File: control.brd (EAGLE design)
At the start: 100 x 80 mm, 60 parts, among them IC1 OPA336P, IC2 XMEGA16A4A, IC3 LM317MBSTT3, IC4 OPA336P, Q1 BSS123, Q2 BSS123, Q3 BC548, Q4 BC557C, Q5 TIP41C, Q6 TIP42C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

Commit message: noch falsche layer
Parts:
- removed IC1, IC4: OPA336P, burr-brown:DIL08
- added C10, C9: (no value), resistor:E2,5-7
- added IC5: LM358N, linear:DIL08
- added R32, R33, R34, R35, R36, R37, R38, R39, R40, R41, R42, R43, R44, R45, R46, R47, R48: (no value), resistor:M0805
- added SV1, SV2: (no value), con-ml:ML6S
- moved C3 65.1 mm to (25.4, 31.8)
- moved C1 64.8 mm to (34.3, 36.8)
- moved JP6 64.3 mm to (8.89, 34.3)
- moved Q5 64.2 mm to (48.3, 7.62), turned to 270 degrees
- moved C2 63.2 mm to (16.5, 39.4)
- moved C4 63.2 mm to (22.9, 48.3)
- moved R18 63.2 mm to (16.5, 44.5)
- moved IC2 63.2 mm to (25.4, 39.4)
- moved Q6 60.2 mm to (48.3, 20.3), turned to 270 degrees
- moved JP4 59.9 mm to (22.9, 29.2)
- moved C7 59.9 mm to (41.9, 3.81), flipped to the bottom
- moved R13 53.0 mm to (41.9, 20.3), flipped to the bottom, turned to 0 degrees
- moved Q7 50.6 mm to (41.9, 16.5)
- moved R10 50.6 mm to (3.81, 45.7)
- moved R7 50.6 mm to (3.81, 49.5)
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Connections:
- removed net N$12: C7.1, Q5.E, R22.1
- new net DIS_A: IC2.20, Q1.1
- new net EN_A1: IC2.21, Q2.1
- new net EN_A2: IC2.22, Q8.1
- new net N$44: IC2.34, SV2.P$1
- net +12V: now also C9.+, IC5.8; no longer IC1.4, IC4.4
- net +3V3: now also SV2.P$2
- net ADC2: now also IC5.2; no longer IC1.2
- net ADC4: now also C10.+, C7.1, Q5.E, R22.1, R32.2
- net GND: now also C10.-, C9.-, IC5.4, R33.1, R34.1, R35.1, R36.1, R37.1, R38.1, R39.1, R40.1, SV2.P$6; no longer IC1.7, IC4.7
- net N$11: now also IC5.3; no longer IC1.3
- net N$17: now also SV2.P$5
- net N$18: now also R33.2, R41.1
- net N$19: now also R34.2, R42.1
- net N$20: now also R35.2, R43.1
- net N$21: now also R36.2, R44.1
- net N$22: now also R37.2, R45.1
- net N$23: now also R38.2, R46.1
- net N$24: now also R39.2, R47.1
- net N$25: now also R40.2, R48.1
- net N$28: now also IC5.7; no longer IC4.6
- net N$30: now also IC5.6; no longer IC4.2
- net N$31: now also IC5.5; no longer IC4.3
- net N$32: now also R32.1
- net N$9: now also IC5.1; no longer IC1.6
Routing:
- net N$32: track 11.7 -> 0.00 mm
- net N$30: track 8.53 -> 0.00 mm
- net N$28: track 8.27 -> 0.00 mm
- net ADC3: track 6.13 -> 14.3 mm
- net +12V: track 26.5 -> 34.0 mm, vias 0 -> 1
- net N$4: track 7.38 -> 0.54 mm
- net N$11: track 13.5 -> 6.94 mm
- net N$7: track 2.54 -> 8.15 mm
- net N$36: track 0.00 -> 5.47 mm, vias 0 -> 1
- net N$12: track 5.18 -> 0.00 mm
- net N$9: track 16.3 -> 21.4 mm
- net N$29: track 12.7 -> 7.62 mm
- net ADC1: track 25.3 -> 20.9 mm
- net N$13: track 4.20 -> 0.00 mm
- net N$34: track 11.2 -> 15.3 mm
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
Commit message: layer korrigiert
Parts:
- removed R10, R11, R12, R14, R15, R7, R8, R9: (no value), resistor:M0805
- removed SV1: (no value), con-ml:ML6S
- moved SV2 133.5 mm to (2.54, 40.6), flipped to the bottom, turned to 270 degrees
- moved R48 104.2 mm to (76.2, 12.7)
- moved R47 103.3 mm to (76.2, 15.2)
- moved R46 102.4 mm to (76.2, 17.8)
- moved R45 101.5 mm to (76.2, 20.3)
- moved R44 100.6 mm to (76.2, 22.9)
- moved R43 99.8 mm to (76.2, 25.4)
- moved R42 98.9 mm to (76.2, 27.9)
- moved R41 98.1 mm to (76.2, 30.5)
- moved R40 81.0 mm to (71.1, 12.7)
- moved R39 80.4 mm to (71.1, 15.2)
- moved R38 79.7 mm to (71.1, 17.8)
- moved R37 79.1 mm to (71.1, 20.3)
- moved R36 78.5 mm to (71.1, 22.9)
- moved R35 77.8 mm to (71.1, 25.4)
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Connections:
- removed net N$10: R14.2, R15.1
- removed net N$2: R11.2, R12.1
- removed net N$3: R10.1, R9.2
- removed net N$5: R7.2, R8.1
- net ADC1: no longer R8.2
- net ADC2: no longer R10.2
- net ADC3: no longer R12.2
- net ADC4: no longer R15.2
- net GND: no longer R11.1, R14.1, R7.1, R9.1
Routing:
- net ADC4: track 15.9 -> 56.1 mm
- net +3V3: track 0.00 -> 37.9 mm
- net +12V: track 34.0 -> 71.6 mm, vias 1 -> 2
- net DIS_A: track 0.00 -> 30.7 mm
- net EN_A1: track 0.00 -> 28.3 mm
- net N$32: track 0.00 -> 17.5 mm
- net EN_A2: track 0.00 -> 17.1 mm
- net N$31: track 0.00 -> 15.5 mm
- net N$4: track 0.54 -> 10.9 mm
- net N$35: track 0.00 -> 9.87 mm, vias 0 -> 1
- net N$6: track 0.00 -> 8.50 mm, vias 0 -> 1
- net N$30: track 0.00 -> 8.44 mm
- net N$1: track 10.6 -> 17.8 mm
- net N$28: track 0.00 -> 6.66 mm
- net N$27: track 0.00 -> 4.83 mm
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
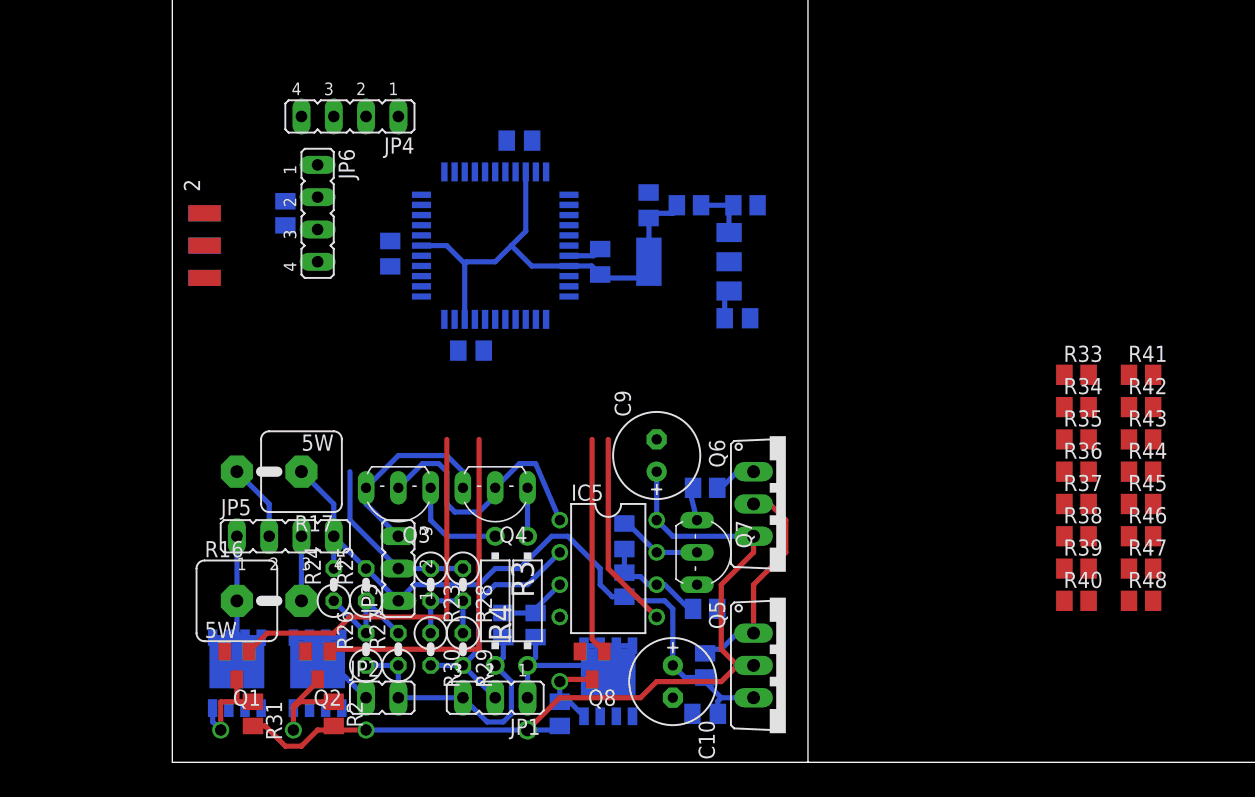
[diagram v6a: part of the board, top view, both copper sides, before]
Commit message: adc angeschlossen
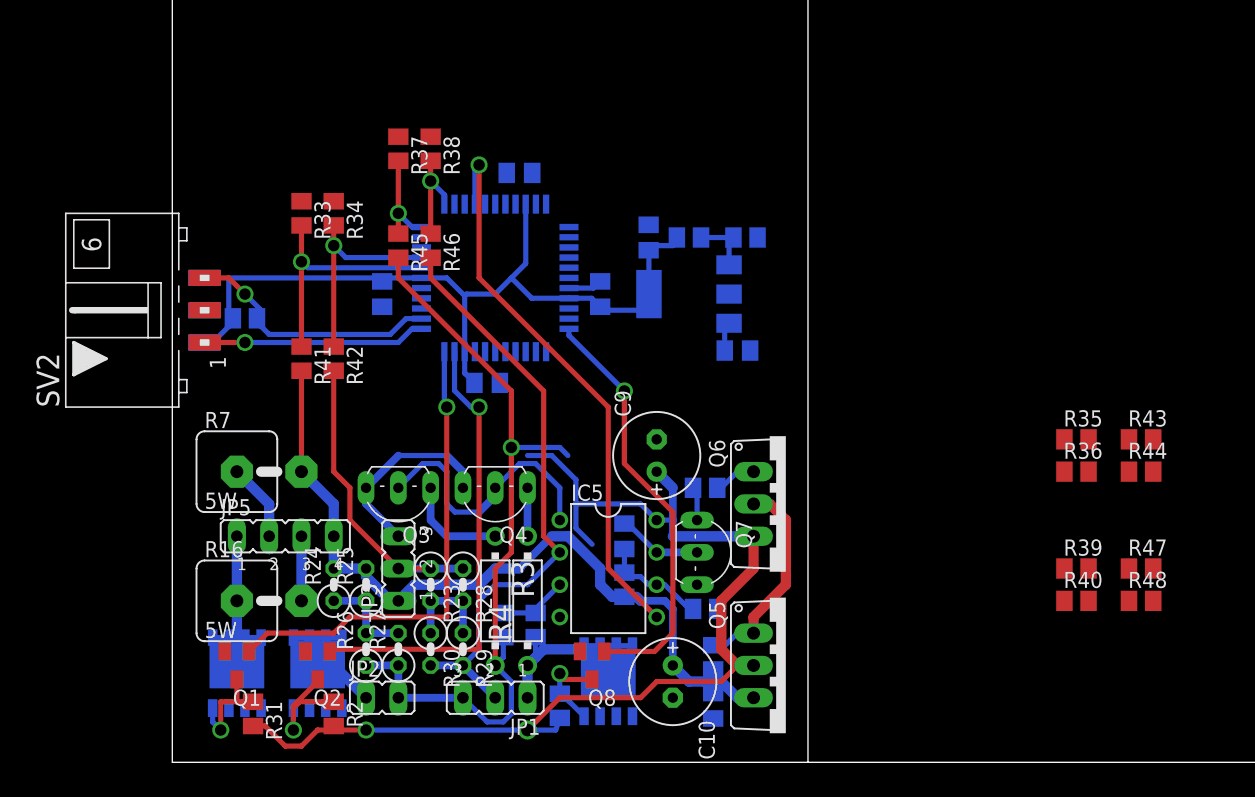
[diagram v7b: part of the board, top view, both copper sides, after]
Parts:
- removed JP4, JP6: (no value), jumper:JP4
- moved R41 66.1 mm to (10.2, 31.8), turned to 270 degrees
- moved R42 63.6 mm to (12.7, 31.8), turned to 270 degrees
- moved R33 62.3 mm to (10.2, 43.2), turned to 270 degrees
- moved R45 61.9 mm to (17.8, 40.6), turned to 270 degrees
- moved R46 60.4 mm to (20.3, 40.6), turned to 270 degrees
- moved R34 60.4 mm to (12.7, 43.2), turned to 270 degrees
- moved R37 60.2 mm to (17.8, 48.3), turned to 270 degrees
- moved R38 59.2 mm to (20.3, 48.3), turned to 270 degrees
- moved R18 8.84 mm to (5.71, 34.9), turned to 0 degrees
- moved SV2 5.08 mm to (2.54, 35.6), flipped to the top, turned to 90 degrees
- moved C2 3.24 mm to (16.5, 36.8)
- moved C3 2.84 mm to (24.8, 29.8)
- moved C4 2.54 mm to (27.3, 46.4)
- moved C1 2.54 mm to (33.7, 36.8)
- moved C5 2.54 mm to (37.5, 41.3)
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- renumbered R17 to R7
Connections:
- new net N$10: R44.2
- new net N$38: R47.2
- new net N$39: R48.2
- new net N$5: R43.2
- net ADC1: now also R45.2
- net ADC2: now also R46.2
- net ADC3: now also R42.2
- net ADC4: now also R41.2, R7.2; no longer R7.1
- net DIS_A: now also IC2.33; no longer IC2.20
- net EN_A1: now also IC2.32; no longer IC2.21
- net N$16: now also R7.1; no longer R7.2
- net N$18: no longer JP6.4
- net N$19: no longer JP6.3
- net N$20: no longer JP6.2
- net N$21: no longer JP6.1
- net N$22: no longer JP4.4
- net N$23: no longer JP4.3
- net N$24: no longer JP4.2
- net N$25: no longer JP4.1
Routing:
- net ADC1: track 21.8 -> 62.8 mm, vias 0 -> 1
- net N$31: track 15.5 -> 44.6 mm, vias 0 -> 1
- net ADC2: track 19.7 -> 47.1 mm
- net +3V3: track 37.9 -> 63.1 mm
- net N$17: track 0.00 -> 20.9 mm, vias 0 -> 1
- net N$18: track 0.00 -> 19.2 mm, vias 0 -> 1
- net +12V: track 71.6 -> 90.5 mm
- net N$44: track 0.00 -> 17.5 mm, vias 0 -> 1
- net N$19: track 0.00 -> 16.8 mm, vias 0 -> 1
- net EN_A2: track 17.1 -> 33.3 mm, vias 0 -> 1
- net ADC3: track 14.3 -> 25.3 mm
- net ADC4: track 56.1 -> 64.2 mm
- net EN_A1: track 28.3 -> 36.4 mm, vias 0 -> 1
- net N$23: track 0.00 -> 7.99 mm, vias 0 -> 1
- net N$22: track 0.00 -> 7.99 mm, vias 0 -> 1
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
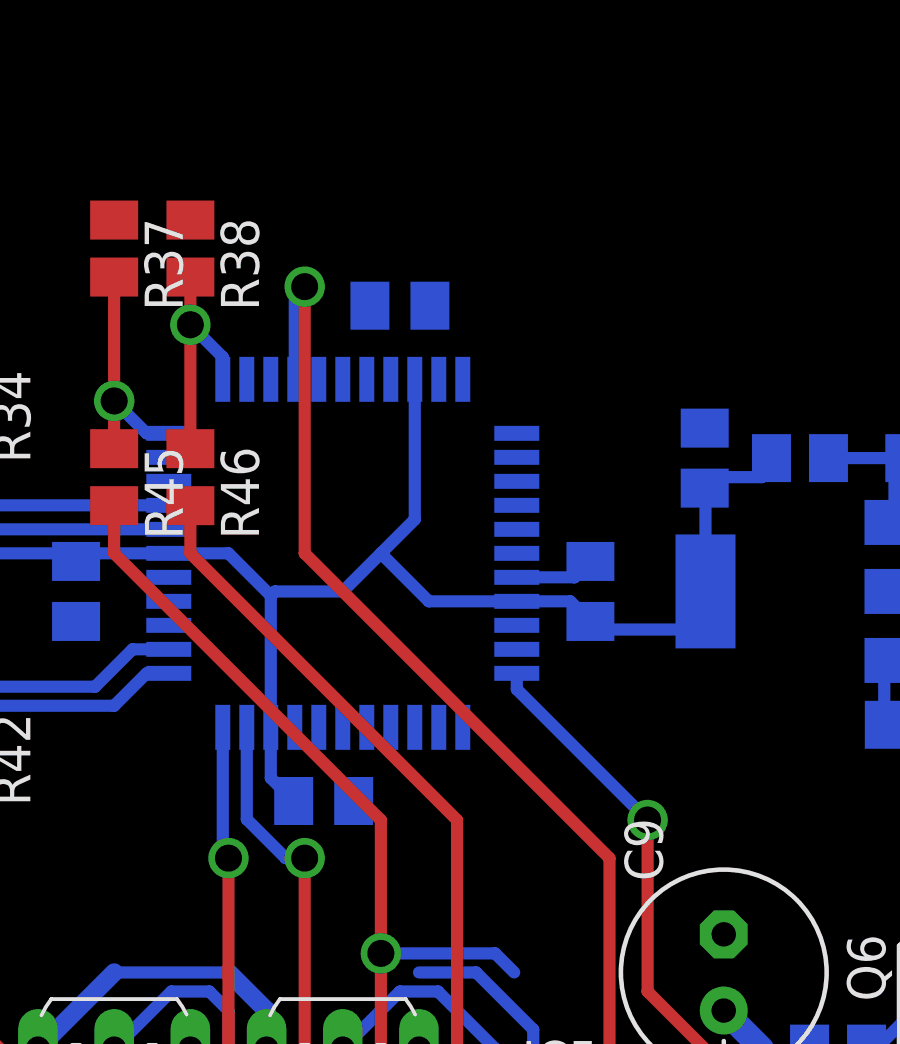
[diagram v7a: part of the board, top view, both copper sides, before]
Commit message: DAC pin corrected
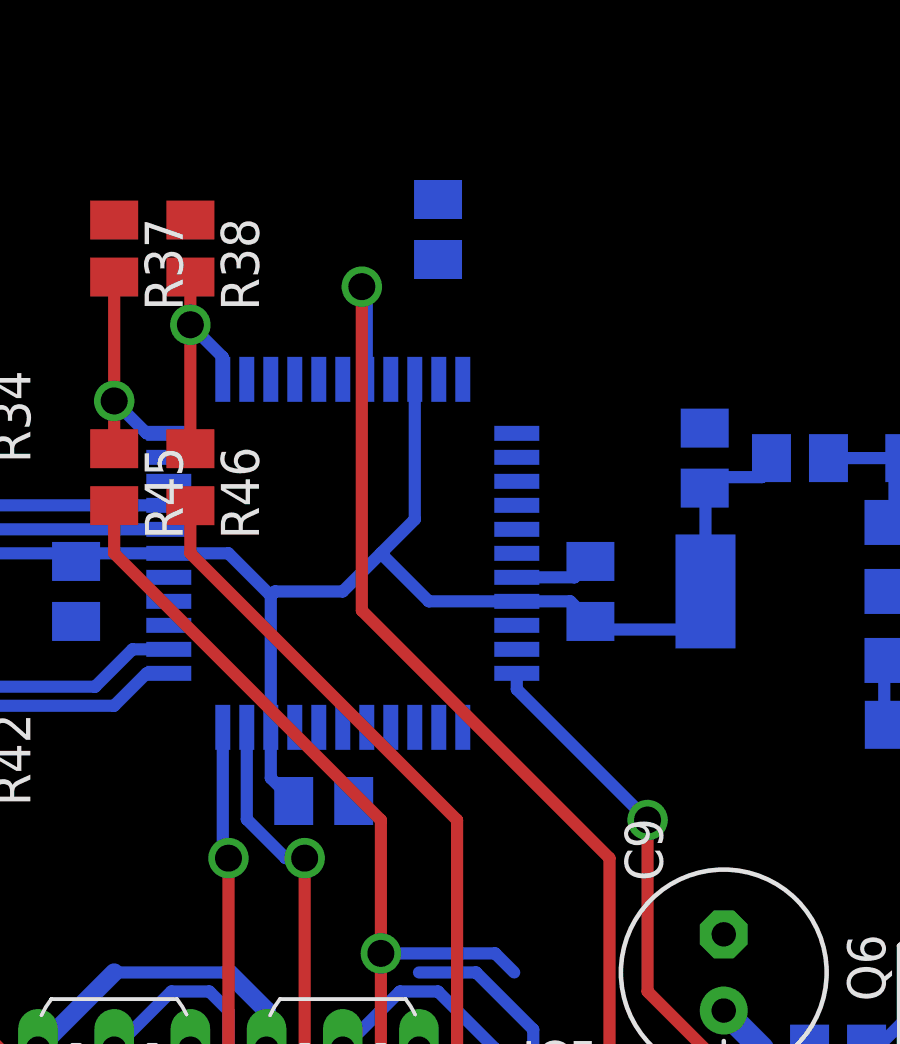
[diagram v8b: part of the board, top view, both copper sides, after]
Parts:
- moved C4 2.84 mm to (28.6, 48.9), turned to 90 degrees
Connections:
- net N$31: now also IC2.7; no longer IC2.4
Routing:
- net N$31: track 44.6 -> 43.8 mm
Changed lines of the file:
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@@
 <element name="C2" library="resistor" package="C0805K" value="" x="16.51" y="36.83" rot="MR270"/>
 <element name="C3" library="resistor" package="C0805K" value="" x="24.765" y="29.845" rot="MR180"/>
-<element name="C4" library="resistor" package="C0805K" value="" x="27.305" y="46.355" rot="MR0"/>
+<element name="C4" library="resistor" package="C0805K" value="" x="28.575" y="48.895" rot="MR90"/>
 <element name="R18" library="resistor" package="M0805" value="" x="5.715" y="34.925" rot="MR0"/>
 <element name="IC3" library="v-reg" package="SOT223" value="LM317MBSTT3" x="40.64" y="36.83" rot="MR270"/>
@@
 <wire x1="33.655" y1="37.83" x2="37.465" y2="42.275" width="0" layer="19" extent="16-16"/>
 <wire x1="27" y1="43.9" x2="31.2" y2="37.3" width="0" layer="19" extent="16-16"/>
-<wire x1="26.305" y1="46.355" x2="27" y2="43.9" width="0" layer="19" extent="16-16"/>
-<wire x1="20.32" y1="49.21" x2="26.305" y2="46.355" width="0" layer="19" extent="1-16"/>
+<wire x1="28.575" y1="49.895" x2="27" y2="43.9" width="0" layer="19" extent="16-16"/>
+<wire x1="20.32" y1="49.21" x2="28.575" y2="49.895" width="0" layer="19" extent="1-16"/>
 <wire x1="17.78" y1="49.21" x2="20.32" y2="49.21" width="0" layer="19" extent="1-1"/>
 <wire x1="12.7" y1="44.13" x2="17.78" y2="49.21" width="0" layer="19" extent="1-1"/>
@@
 <wire x1="4.765" y1="34.925" x2="4.765" y2="34.61" width="0.4064" layer="16"/>
 <wire x1="4.765" y1="34.61" x2="4.445" y2="34.29" width="0.4064" layer="16"/>
-<wire x1="27.8" y1="43.9" x2="28.305" y2="46.355" width="0" layer="19" extent="16-16"/>
+<wire x1="27.8" y1="43.9" x2="28.575" y2="47.895" width="0" layer="19" extent="16-16"/>
 </signal>
 <signal name="N$17">
@@
 </signal>
 <signal name="N$31">
-<contactref element="IC2" pad="4"/>
 <contactref element="IC5" pad="5"/>
 <wire x1="38.1" y1="11.43" x2="34.29" y2="15.24" width="0.4064" layer="1"/>
 <wire x1="34.29" y1="15.24" x2="34.29" y2="27.94" width="0.4064" layer="1"/>
-<wire x1="34.29" y1="27.94" x2="24.13" y2="38.1" width="0.4064" layer="1"/>
-<wire x1="24.13" y1="38.1" x2="24.13" y2="46.99" width="0.4064" layer="1"/>
-<via x="24.13" y="46.99" extent="1-16" drill="0.9" shape="octagon"/>
-<wire x1="24.13" y1="46.99" x2="23.8" y2="46.66" width="0.4064" layer="16"/>
-<wire x1="23.8" y1="46.66" x2="23.8" y2="43.9" width="0.4064" layer="16"/>
+<wire x1="34.29" y1="27.94" x2="26.035" y2="36.195" width="0.4064" layer="1"/>
+<wire x1="26.035" y1="36.195" x2="26.035" y2="46.99" width="0.4064" layer="1"/>
+<via x="26.035" y="46.99" extent="1-16" drill="0.9" shape="octagon"/>
+<contactref element="IC2" pad="7"/>
+<wire x1="26.035" y1="46.99" x2="26.2" y2="46.99" width="0.4064" layer="16"/>
+<wire x1="26.2" y1="46.99" x2="26.2" y2="43.9" width="0.4064" layer="16"/>
 </signal>
 <signal name="N$32">
